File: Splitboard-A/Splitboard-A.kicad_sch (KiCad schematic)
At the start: 116 parts, among them J1 USB_C_Receptacle_USB2.0, J2 USB_C_Receptacle, J3 Conn_01x07, K1 KEYSW, K10 KEYSW, K11 KEYSW, K12 KEYSW, K13 KEYSW, K14 KEYSW, K15 KEYSW, K16 KEYSW, K17 KEYSW, K18 KEYSW, K19 KEYSW, K2 KEYSW, K20 KEYSW, K21 KEYSW, K22 KEYSW, K23 KEYSW, K24 KEYSW, K25 KEYSW, K26 KEYSW, K27 KEYSW, K28 KEYSW, K29 KEYSW, K3 KEYSW, K30 KEYSW, K31 KEYSW, K32 KEYSW, K33 KEYSW, K34 KEYSW, K35 KEYSW, K36 KEYSW, K37 KEYSW, K38 KEYSW, K4 KEYSW, K5 KEYSW, K6 KEYSW, K7 KEYSW, K8 KEYSW, K9 KEYSW, SW2 SW_Push, U1 AMS1117-3.3, U2 STM32F407VGTx, U3 CR2013-MI2120

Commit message: keyboard layout changes
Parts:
- renumbered D4 to D1, D13 to D10, D14 to D11, D15 to D12, D16 to D13, D17 to D14, D18 to D15, D19 to D16, D20 to D17, D21 to D18, D22 to D19, D5 to D2, D23 to D20, D24 to D21, D25 to D22, D26 to D23, D27 to D24, D28 to D25, D29 to D26, D30 to D27, D31 to D28, D32 to D29, D6 to D3, D33 to D30, D34 to D31, D35 to D32, D36 to D33, D37 to D34, D38 to D35, D39 to D36, D40 to D37, D41 to D38, D7 to D4, D1 to D40, D2 to D41, D3 to D42, D8 to D5, D9 to D6, D10 to D7, D11 to D8, D12 to D9

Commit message: layout updates
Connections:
- net +3.3V: no longer C1.1, C3.1, D41.2 (A), D42.1 (K), R2.1, U1.2 (VO)
- new net +3v3 to micro: C1.1, C3.1, D41.2 (A), D42.1 (K), R2.1, U1.2 (VO)
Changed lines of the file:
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@@
   (junction (at 494.03 355.6) (diameter 0) (color 0 0 0 0)
   )
-  (junction (at 87.376 139.954) (diameter 0) (color 0 0 0 0)
-  )
   (junction (at 269.24 115.57) (diameter 0) (color 0 0 0 0)
   )
@@
     (stroke (width 0) (type default) (color 0 0 0 0))
   )
-  (wire (pts (xy 82.804 139.954) (xy 87.376 139.954))
+  (wire (pts (xy 82.804 139.954) (xy 93.218 139.954))
     (stroke (width 0) (type default) (color 0 0 0 0))
   )
@@
     (stroke (width 0) (type default) (color 0 0 0 0))
   )
-  (wire (pts (xy 87.376 139.954) (xy 93.218 139.954))
-    (stroke (width 0) (type default) (color 0 0 0 0))
-  )
   (wire (pts (xy 463.55 235.458) (xy 463.55 236.728))
     (stroke (width 0) (type default) (color 0 0 0 0))
@@
     (effects (font (size 1.27 1.27)) (justify left bottom))
   )
-  (label "3V3" (at 62.738 369.57 0)
+  (label "3V-USB" (at 62.738 369.57 0)
     (effects (font (size 1.27 1.27)) (justify left bottom))
   )
@@
     (effects (font (size 1.27 1.27)) (justify left bottom))
   )
+  (label "3V-USB" (at 84.836 139.954 0)
+    (effects (font (size 1.27 1.27)) (justify left bottom))
+  )
   (label "SWDIO" (at 339.598 330.708 0)
     (effects (font (size 1.27 1.27)) (justify left bottom))
@@
     (effects (font (size 1.27 1.27)) (justify left bottom))
   )
-  (label "3V3" (at 136.652 276.606 0)
-    (effects (font (size 1.27 1.27)) (justify left bottom))
-  )
   (label "row1" (at 416.56 178.308 180)
     (effects (font (size 1.27 1.27)) (justify right bottom))
@@
     (pin "2")
   )
-  (symbol (lib_id "power:+3.3V") (at 87.376 139.954 0) (unit 1)
-    (in_bom yes) (on_board yes) (fields_autoplaced)
-    (property "Reference" "#PWR04" (id 0) (at 87.376 143.764 0)
-      (effects (font (size 1.27 1.27)) hide)
-    )
-    (property "Value" "+3.3V" (id 1) (at 87.376 134.874 0))
-    (property "Footprint" "" (id 2) (at 87.376 139.954 0)
-      (effects (font (size 1.27 1.27)) hide)
-    )
-    (property "Datasheet" "" (id 3) (at 87.376 139.954 0)
-      (effects (font (size 1.27 1.27)) hide)
-    )
-    (pin "1")
-  )
   (symbol (lib_id "KBT1-rescue:D-Device") (at 485.14 250.698 90) (unit 1)
     (in_bom yes) (on_board yes)
@@
       (reference "#PWR03") (unit 1) (value "+3.3V") (footprint "")
     )
-    (path "/437506f4-9c95-4981-b82e-2fe5deb41c0d"
-      (reference "#PWR04") (unit 1) (value "+3.3V") (footprint "")
-    )
     (path "/661a6976-5c5b-4e1c-82b9-30cd8398a1f3"

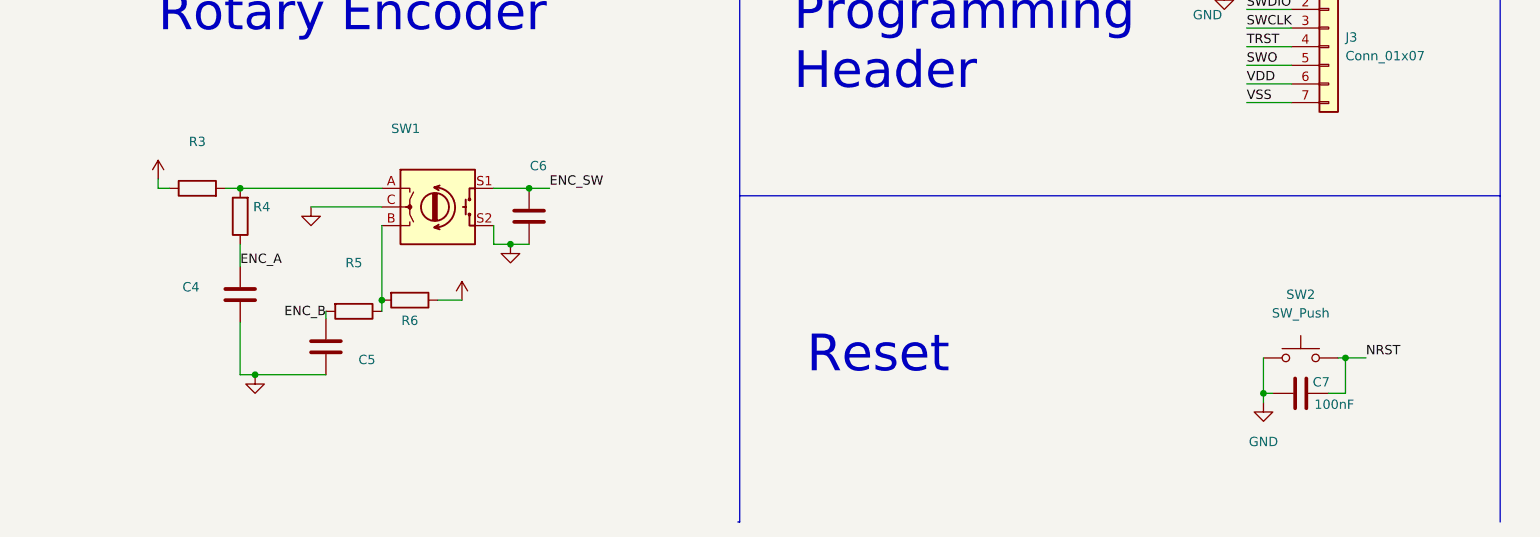
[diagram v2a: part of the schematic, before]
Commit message: Added switch footprint (6x6mm)
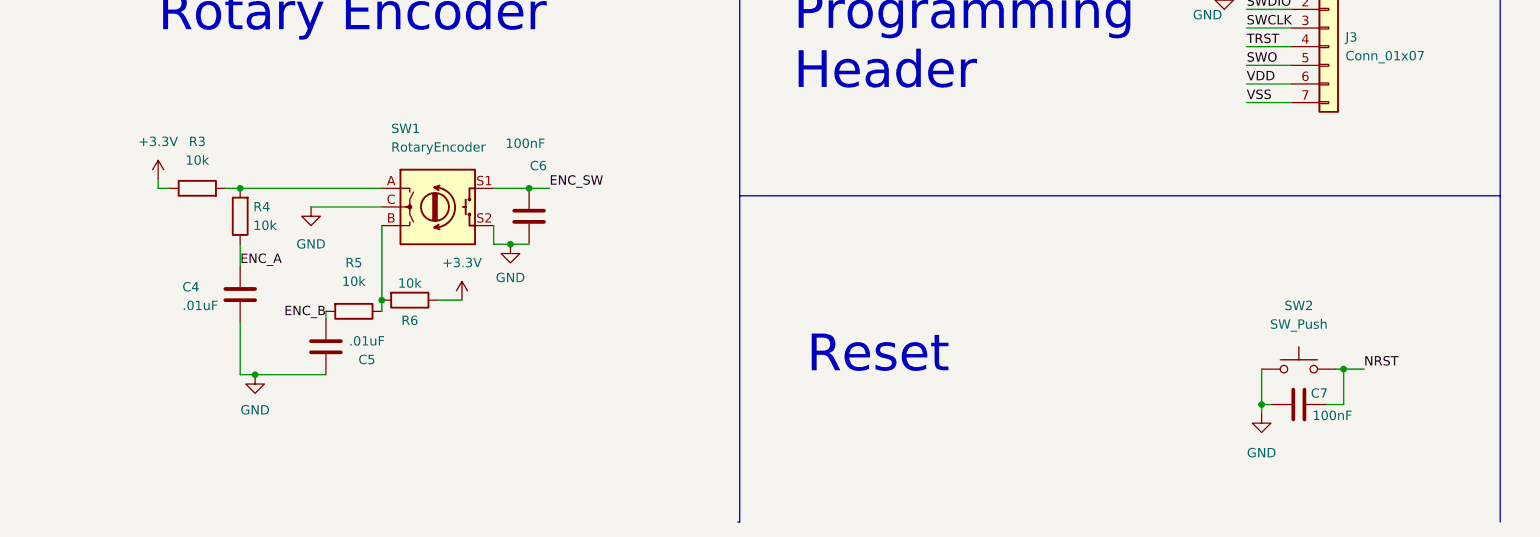
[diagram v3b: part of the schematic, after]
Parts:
- C4, C5: value (none) -> .01uF
- C6: value (none) -> 100nF
- R3, R4, R5, R6: value (none) -> 10k
- SW1: value (none) -> RotaryEncoder; footprint (none) -> Rotary_Encoder:RotaryEncoder_Alps_EC12E_Vertical_H20mm
- SW2: footprint Button_Switch_SMD:Nidec_Copal_SH-7010A -> Button_Switch_THT:SW_PUSH_6mm
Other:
- moved on the sheet: C7, SW2
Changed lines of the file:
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@@
   (junction (at 501.65 206.248) (diameter 0) (color 0 0 0 0)
   )
-  (junction (at 341.884 383.032) (diameter 0) (color 0 0 0 0)
+  (junction (at 341.63 384.556) (diameter 0) (color 0 0 0 0)
   )
   (junction (at 480.06 245.618) (diameter 0) (color 0 0 0 0)
@@
   (junction (at 481.584 355.6) (diameter 0) (color 0 0 0 0)
   )
-  (junction (at 353.06 378.206) (diameter 0) (color 0 0 0 0)
+  (junction (at 352.806 379.73) (diameter 0) (color 0 0 0 0)
   )
   (junction (at 457.2 245.618) (diameter 0) (color 0 0 0 0)
@@
     (stroke (width 0) (type default) (color 0 0 0 0))
   )
-  (wire (pts (xy 353.06 383.032) (xy 353.06 378.206))
+  (wire (pts (xy 352.806 384.556) (xy 352.806 379.73))
     (stroke (width 0) (type default) (color 0 0 0 0))
   )
@@
     (stroke (width 0) (type default) (color 0 0 0 0))
   )
-  (wire (pts (xy 350.774 383.032) (xy 353.06 383.032))
+  (wire (pts (xy 350.52 384.556) (xy 352.806 384.556))
     (stroke (width 0) (type default) (color 0 0 0 0))
   )
@@
     (stroke (width 0) (type default) (color 0 0 0 0))
   )
-  (wire (pts (xy 341.884 383.032) (xy 343.154 383.032))
+  (wire (pts (xy 341.63 384.556) (xy 342.9 384.556))
     (stroke (width 0) (type default) (color 0 0 0 0))
   )
@@
     (stroke (width 0) (type default) (color 0 0 0 0))
   )
-  (wire (pts (xy 355.854 378.206) (xy 353.06 378.206))
+  (wire (pts (xy 355.6 379.73) (xy 352.806 379.73))
     (stroke (width 0) (type default) (color 0 0 0 0))
   )
@@
     (stroke (width 0) (type default) (color 0 0 0 0))
   )
-  (wire (pts (xy 353.06 378.206) (xy 352.044 378.206))
+  (wire (pts (xy 352.806 379.73) (xy 351.79 379.73))
     (stroke (width 0) (type default) (color 0 0 0 0))
   )
@@
     (stroke (width 0) (type default) (color 0 0 0 0))
   )
-  (wire (pts (xy 341.884 378.206) (xy 341.884 383.032))
+  (wire (pts (xy 341.63 379.73) (xy 341.63 384.556))
     (stroke (width 0) (type default) (color 0 0 0 0))
   )
@@
     (stroke (width 0) (type default) (color 0 0 0 0))
   )
-  (wire (pts (xy 341.884 383.032) (xy 341.884 384.302))
+  (wire (pts (xy 341.63 384.556) (xy 341.63 385.826))
     (stroke (width 0) (type default) (color 0 0 0 0))
   )
@@
     (effects (font (size 4 4)) (justify left bottom))
   )
-  (label "NRST" (at 355.854 378.206 0)
+  (label "NRST" (at 355.6 379.73 0)
     (effects (font (size 1.27 1.27)) (justify left bottom))
   )
@@
       (effects (font (size 1.27 1.27)) hide)
     )
-    (property "Value" "" (id 1) (at 232.664 365.252 0))
+    (property "Value" "+3.3V" (id 1) (at 232.664 365.252 0))
     (property "Footprint" "" (id 2) (at 232.664 370.332 0)
       (effects (font (size 1.27 1.27)) hide)
@@
     (pin "2")
   )
-  (symbol (lib_id "power:GND") (at 341.884 384.302 0) (unit 1)
+  (symbol (lib_id "power:GND") (at 341.63 385.826 0) (unit 1)
     (in_bom yes) (on_board yes) (fields_autoplaced)
-    (property "Reference" "#PWR017" (id 0) (at 341.884 390.652 0)
+    (property "Reference" "#PWR017" (id 0) (at 341.63 392.176 0)
       (effects (font (size 1.27 1.27)) hide)
     )
-    (property "Value" "GND" (id 1) (at 341.884 389.636 0))
-    (property "Footprint" "" (id 2) (at 341.884 384.302 0)
+    (property "Value" "GND" (id 1) (at 341.63 391.16 0))
+    (property "Footprint" "" (id 2) (at 341.63 385.826 0)
       (effects (font (size 1.27 1.27)) hide)
     )
-    (property "Datasheet" "" (id 3) (at 341.884 384.302 0)
+    (property "Datasheet" "" (id 3) (at 341.63 385.826 0)
       (effects (font (size 1.27 1.27)) hide)
     )
@@
       (effects (font (size 1.27 1.27)) hide)
     )
-    (property "Value" "" (id 1) (at 204.47 385.318 0))
+    (property "Value" "GND" (id 1) (at 204.47 385.318 0))
     (property "Footprint" "" (id 2) (at 204.47 380.492 0)
       (effects (font (size 1.27 1.27)) hide)
@@
       (effects (font (size 1.27 1.27)) (justify left))
     )
-    (property "Value" "" (id 1) (at 223.012 349.504 0)
+    (property "Value" "RotaryEncoder" (id 1) (at 223.012 349.504 0)
       (effects (font (size 1.27 1.27)) (justify left))
     )
-    (property "Footprint" "" (id 2) (at 225.552 353.568 0)
+    (property "Footprint" "Rotary_Encoder:RotaryEncoder_Alps_EC12E_Vertical_H20mm" (id 2) (at 225.552 353.568 0)
       (effects (font (size 1.27 1.27)) hide)
     )
@@
     (pin "2")
   )
-  (symbol (lib_id "Device:C") (at 346.964 383.032 90) (unit 1)
+  (symbol (lib_id "Device:C") (at 346.71 384.556 90) (unit 1)
     (in_bom yes) (on_board yes)
-    (property "Reference" "C7" (id 0) (at 349.758 381.508 90))
-    (property "Value" "100nF" (id 1) (at 351.536 384.556 90))
-    (property "Footprint" "Capacitor_SMD:C_0805_2012Metric" (id 2) (at 350.774 382.0668 0)
+    (property "Reference" "C7" (id 0) (at 349.504 383.032 90))
+    (property "Value" "100nF" (id 1) (at 351.282 386.08 90))
+    (property "Footprint" "Capacitor_SMD:C_0805_2012Metric" (id 2) (at 350.52 383.5908 0)
       (effects (font (size 1.27 1.27)) hide)
     )
-    (property "Datasheet" "~" (id 3) (at 346.964 383.032 0)
+    (property "Datasheet" "~" (id 3) (at 346.71 384.556 0)
       (effects (font (size 1.27 1.27)) hide)
     )
@@
     (in_bom yes) (on_board yes)
     (property "Reference" "C6" (id 0) (at 243.078 352.044 0))
-    (property "Value" "" (id 1) (at 241.3 348.996 0))
+    (property "Value" "100nF" (id 1) (at 241.3 348.996 0))
     (property "Footprint" "Capacitor_SMD:C_0805_2012Metric" (id 2) (at 240.8428 355.092 0)
       (effects (font (size 1.27 1.27)) hide)
@@
     (in_bom yes) (on_board yes) (fields_autoplaced)
     (property "Reference" "R3" (id 0) (at 196.596 348.742 90))
-    (property "Value" "" (id 1) (at 196.596 351.282 90))
+    (property "Value" "10k" (id 1) (at 196.596 351.282 90))
     (property "Footprint" "Resistor_SMD:R_0805_2012Metric" (id 2) (at 196.596 356.87 90)
       (effects (font (size 1.27 1.27)) hide)
@@
     (in_bom yes) (on_board yes)
     (property "Reference" "C5" (id 0) (at 219.71 378.46 0))
-    (property "Value" "" (id 1) (at 219.71 375.92 0))
+    (property "Value" ".01uF" (id 1) (at 219.71 375.92 0))
     (property "Footprint" "Capacitor_SMD:C_0805_2012Metric" (id 2) (at 213.1568 372.872 0)
       (effects (font (size 1.27 1.27)) hide)
@@
       (effects (font (size 1.27 1.27)) (justify left))
     )
-    (property "Value" "" (id 1) (at 194.564 371.094 0)
+    (property "Value" ".01uF" (id 1) (at 194.564 371.094 0)
       (effects (font (size 1.27 1.27)) (justify left))
     )
@@
     (in_bom yes) (on_board yes) (fields_autoplaced)
     (property "Reference" "R5" (id 0) (at 217.932 365.252 90))
-    (property "Value" "" (id 1) (at 217.932 367.792 90))
+    (property "Value" "10k" (id 1) (at 217.932 367.792 90))
     (property "Footprint" "Resistor_SMD:R_0805_2012Metric" (id 2) (at 217.932 370.078 90)
       (effects (font (size 1.27 1.27)) hide)
@@
     (in_bom yes) (on_board yes)
     (property "Reference" "R6" (id 0) (at 225.552 373.126 90))
-    (property "Value" "" (id 1) (at 225.552 368.046 90))
+    (property "Value" "10k" (id 1) (at 225.552 368.046 90))
     (property "Footprint" "Resistor_SMD:R_0805_2012Metric" (id 2) (at 225.552 368.554 90)
       (effects (font (size 1.27 1.27)) hide)
@@
     (pin "1")
   )
-  (symbol (lib_id "Switch:SW_Push") (at 346.964 378.206 0) (unit 1)
-    (in_bom yes) (on_board yes) (fields_autoplaced)
-    (property "Reference" "SW2" (id 0) (at 346.964 369.57 0))
-    (property "Value" "SW_Push" (id 1) (at 346.964 372.11 0))
-    (property "Footprint" "Button_Switch_SMD:Nidec_Copal_SH-7010A" (id 2) (at 346.964 373.126 0)
+  (symbol (lib_id "Switch:SW_Push") (at 346.71 379.73 0) (unit 1)
+    (in_bom yes) (on_board yes)
+    (property "Reference" "SW2" (id 0) (at 346.71 371.094 0))
+    (property "Value" "SW_Push" (id 1) (at 346.71 373.634 0))
+    (property "Footprint" "Button_Switch_THT:SW_PUSH_6mm" (id 2) (at 346.71 375.92 0)
       (effects (font (size 1.27 1.27)) hide)
     )
-    (property "Datasheet" "~" (id 3) (at 346.964 373.126 0)
+    (property "Datasheet" "~" (id 3) (at 346.71 374.65 0)
       (effects (font (size 1.27 1.27)) hide)
     )
@@
       (effects (font (size 1.27 1.27)) (justify right))
     )
-    (property "Value" "" (id 1) (at 204.216 360.1719 0)
+    (property "Value" "10k" (id 1) (at 204.216 360.1719 0)
       (effects (font (size 1.27 1.27)) (justify right))
     )
@@
       (effects (font (size 1.27 1.27)) hide)
     )
-    (property "Value" "" (id 1) (at 212.09 362.712 0))
+    (property "Value" "GND" (id 1) (at 212.09 362.712 0))
     (property "Footprint" "" (id 2) (at 212.09 357.632 0)
       (effects (font (size 1.27 1.27)) hide)
@@
       (effects (font (size 1.27 1.27)) hide)
     )
-    (property "Value" "" (id 1) (at 239.268 367.284 0))
+    (property "Value" "GND" (id 1) (at 239.268 367.284 0))
     (property "Footprint" "" (id 2) (at 239.268 362.712 0)
       (effects (font (size 1.27 1.27)) hide)
@@
       (effects (font (size 1.27 1.27)) hide)
     )
-    (property "Value" "" (id 1) (at 191.262 348.742 0))
+    (property "Value" "+3.3V" (id 1) (at 191.262 348.742 0))
     (property "Footprint" "" (id 2) (at 191.262 353.822 0)
       (effects (font (size 1.27 1.27)) hide)
@@
     )
     (path "/aae1d1b8-ecea-4dc3-9e3b-62424a309ff4"
-      (reference "SW2") (unit 1) (value "SW_Push") (footprint "Button_Switch_SMD:Nidec_Copal_SH-7010A")
+      (reference "SW2") (unit 1) (value "SW_Push") (footprint "Button_Switch_THT:SW_PUSH_6mm")
     )
     (path "/a2c78482-cb0c-4264-ab7b-4496795fc80b"

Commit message: Added Joe's suggestions & notes to schematic & pcb
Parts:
- removed J3: Conn_01x07, Connector_PinHeader_2.54mm:PinHeader_1x07_P2.54mm_Horizontal, symbol Connector_Generic:Conn_01x07
- added J?: Conn_01x06, Connector_PinHeader_2.54mm:PinHeader_1x06_P2.54mm_Horizontal, symbol Connector_Generic:Conn_01x06
- added R? (x7): 10k, Resistor_SMD:R_0805_2012Metric, symbol Device:R
- added R? (x2): 5K1, symbol Device:R
- added R?: 10K, symbol Device:R
- C8: value 1uf -> 10uf
- R2: value 100K -> 10
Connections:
- net +3v3 to micro is gone; now on net +3.3V: C1.1, C3.1, D41.2 (A), D42.1 (K), R2.1, U1.2 (VO)
- net +3.3V: now also U2.21 (VREF+), U2.22 (VDDA), U2.6 (VBAT), J?.1 (Pin_1), R?.1, R?.2, R?.2, R?.2, R?.2, R?.2, R?.2, R?.2; no longer J2.A4 (VBUS), J2.A9 (VBUS), J2.B4 (VBUS), J2.B9 (VBUS), R1.2, R2.2
- net ENC_SW: now also R?.1
- net GND: now also J?.3 (Pin_3), R?.2, R?.2
- net NRST: now also J?.5 (Pin_5), R?.2
- net SWCLK: now also J?.2 (Pin_2)
- net SWDIO: now also J?.4 (Pin_4)
- net SWO: now also J?.6 (Pin_6)
- net col0: now also R?.1
- net col1: now also R?.1
- net col2: now also R?.1
- net col3: now also R?.1
- net col4: now also R?.1
- net col5: now also R?.1
- net at J1.A5 (CC1): now also R?.1
- net at J1.B5 (CC2): now also R?.1
- net Voltage Regulator Input renamed VBUS
- net VBUS: now also J2.A4 (VBUS), J2.A9 (VBUS), J2.B4 (VBUS), J2.B9 (VBUS), R1.2, R2.2; no longer D40.2 (A)
- no-connect marks 10 -> 8
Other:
- note added: "10K pullup resistors in case internal don't work"
- note added: "Can likely be replaced by an IC"
- note added: "Fuse not necessary but would need x5 standard current draw"
- note added: "I don't think this connector needs the pull downs on cc1 & cc2 since not real USB"
- note added: "Oscillator"
- note added: "SWO: Serial Wire Output"
- note added: "This likely doesn't need ESD protection, if we want something we can throw small resistors in series with the signals (10 ohms)"
- note added: "Want ESD protection for PC connector, they make a chip that sits on D+ & D-"
- note added: "boot0 needs low boot 1 needs high want boot from internal flash (double check this)"
- note added: "idk ahhhhhhh"
- note added: "needs pulled high 10k"
- note added: "vcap_x both need caps (find values)"
- moved on the sheet: C11, C15, C2, C3, C4, C5, C6, C7, D1, D10, D11, D12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

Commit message: updated USB, LCD, ESD, Voltage Reg in schematic
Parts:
- removed C1: 0.1uF, Resistor_SMD:R_0805_2012Metric, symbol Device:C
- removed D41, D42: D_Schottky, Diode_SMD:D_SOD-123, symbol Device:D_Schottky
- removed F1: 500mA, Fuse:Fuse_BelFuse_0ZRE0125FF_L21.2mm_W5.3mm, symbol Device:Fuse
- removed R1: 10K, Resistor_SMD:R_0805_2012Metric, symbol Device:R
- removed R2: 10, Resistor_SMD:R_0805_2012Metric, symbol Device:R
- added C? (x2): 2u2, symbol Device:C
- added R?: 10k, Resistor_SMD:R_0805_2012Metric, symbol Device:R
- added U?: USBUF02W6, SOTT323-6L_STM, symbol USBUF02W6:USBUF02W6
- J2: footprint Connector_USB:USB_C_Receptacle_GCT_USB4085 -> Connector_USB:USB_C_Receptacle_Amphenol_12401548E4-2A
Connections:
- net +3.3V: now also U3.8 (LED), R?.2, U?.5 (VDD); no longer U3.1 (VCC)
- net ENC_SW: now also R?.1
- net GND: now also U2.20 (VSSA), U2.94 (BOOT0), C?.2, C?.2, U?.2 (GND)
- net LCD1_CS: now also U3.3 (~{CS})
- net LCD1_DC: now also U3.5 (D/~{C})
- net LCD1_RESET: now also U3.4 (RESET)
- net LCD2_CS: now also J2.A10 (RX2-), J2.B10 (RX1-)
- net LCD2_DC: now also J2.A11 (RX2+), J2.B11 (RX1+)
- net MOSI: now also J2.A5 (CC1), J2.B5 (CC2); no longer J2.B11 (RX1+)
- net SCK: now also J2.A8 (SBU1), J2.B8 (SBU2); no longer J2.A2 (TX1+)
- net SCL: now also J2.A7 (D-), J2.B7 (D-); no longer J2.A10 (RX2-)
- net SDA: now also J2.A6 (D+), J2.B6 (D+); no longer J2.A11 (RX2+)
- net VBUS: now also D40.2 (A), U3.1 (VCC)
- net USB_CONN_D+: now reaches J1.B6 (D+)
- net USB_CONN_D+: now also J1.A6 (D+), U?.1 (D1)
- net USB_CONN_D-: now reaches J1.B7 (D-)
- net USB_CONN_D-: now also J1.A7 (D-), U?.3 (D2)
- net at D40.1 (K): now also FB1.1
- net at U2.49 (VCAP_1): now also C?.1
- net at U2.73 (VCAP_2): now also C?.1
- net LCD2_RST: now reaches J2.B3 (TX2-)
- net LCD2_RST: now also J2.A3 (TX1-)
- removed net CS: J2.B10 (RX1-), U3.3 (~{CS})
- net MISO: no longer names the net of U3.9 (MISO)
- net MISO: no longer J2.A3 (TX1-)
- net TRST: no longer names the net of U2.90 (PB4)
- net USB_DM renamed USB_D-
- net USB_D-: now also U?.4 (D3); no longer J1.A7 (D-)
- net USB_DP renamed USB_D+
- net USB_D+: now also U?.6 (D4); no longer J1.A6 (D+)
- no-connect marks 8 -> 10
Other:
- note added: "ESD Protection (data line)"
- note added: "Need to make sure this is all symmetrical"
- note removed: "Can likely be replaced by an IC"
- note removed: "ESD Protection"
- note removed: "Fuse not necessary but would need x5 standard current draw"
- note removed: "Want ESD protection for PC connector, they make a chip that sits on D+ & D-"
- note removed: "boot0 needs low boot 1 needs high want boot from internal flash (double check this)"
- note removed: "idk ahhhhhhh"
- note removed: "vcap_x both need caps (find values)"
- moved on the sheet: C2, C3, D40, FB1, U1

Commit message: assigned new component footprints
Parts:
- added U1: SIT2024BA-S2-33E-8.000000G, SIT2024BA:SIT2024BA-S2-33E-8.000000G, symbol SIT2024BA:SIT2024BA-S2-33E-8.000000G
- C1, C2: renamed from C?; footprint (none) -> Capacitor_SMD:C_0805_2012Metric
- R1, R15, R2: renamed from R?; footprint (none) -> Resistor_SMD:R_0805_2012Metric
- U5: renamed from U?; footprint SOTT323-6L_STM -> ul_USBUF02W6:USBUF02W6
- gave numbers to parts that had none: 9
- renumbered C12 to C10, C13 to C11, C14 to C12, C15 to C13, C16 to C14, C17 to C15, C4 to C16, C5 to C17, C7 to C18, C2 to C3, C3 to C4, C6 to C5, C8 to C6, C9 to C7, C10 to C8, C11 to C9, D23 to D10, D30 to D11, D37 to D12, D3 to D13, D10 to D14, D17 to D15, D24 to D16, D31 to D17, D38 to D18, D4 to D19, D8 to D2, D11 to D20, D18 to D21, D25 to D22, D32 to D23, D5 to D24, D12 to D25, D19 to D26, D26 to D27, D33 to D28, D6 to D29, D15 to D3, D13 to D30, D20 to D31, D27 to D32, D34 to D33, D40 to D34, D7 to D35, D14 to D36, D21 to D37, D28 to D38, D35 to D39, D22 to D4, D29 to D5, D36 to D6, D2 to D7, D9 to D8, D16 to D9, K23 to K10, K30 to K11, K37 to K12, K3 to K13, K10 to K14, K17 to K15, K24 to K16, K31 to K17, K38 to K18, K4 to K19, K8 to K2, K11 to K20, K18 to K21, K25 to K22, K32 to K23, K5 to K24, K12 to K25, K19 to K26, K26 to K27, K33 to K28, K6 to K29, K15 to K3, K13 to K30, K20 to K31, K27 to K32, K34 to K33, K7 to K34, K14 to K35, K21 to K36, K28 to K37, K35 to K38, K22 to K4, K29 to K5, K36 to K6, K2 to K7, K9 to K8, K16 to K9, R3 to R11, R4 to R12, R6 to R13, R5 to R14, U3 to U2, U2 to U3, U1 to U4
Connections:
- net +3.3V: now also U1.4 (VDD)
- net GND: now also U1.1 (GND)
- net RCC_OSC_IN: now reaches U3.12 (PH0)
- net RCC_OSC_IN: now also U1.5 (OUT)
- net RCC_OSC_OUT: now reaches U3.13 (PH1)
- no-connect marks 10 -> 13
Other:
- note added: "8MHz Oscillator"
- note added: "Does this need decoupling caps?"
- note added: "I have no clue what this circuitry should look like"
- note added: "I think this is a N/C but just give this a debugging via"
- note removed: "Oscillator"
